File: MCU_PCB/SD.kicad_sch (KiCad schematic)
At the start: 2 parts

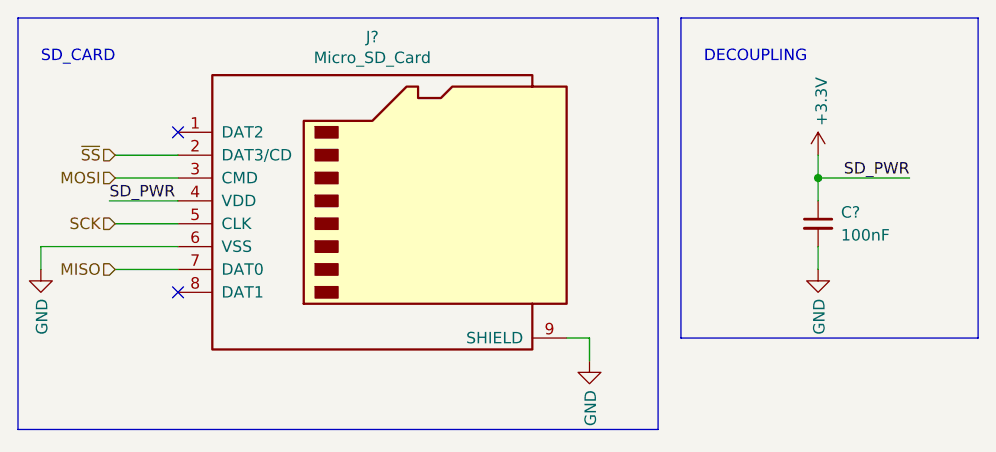
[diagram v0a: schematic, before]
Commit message: 0.1v MCU KiCad
Aesthetics needs to be improved.
Trace width needs to be changed.
More sufficient grounding.
Component placement could be changed.
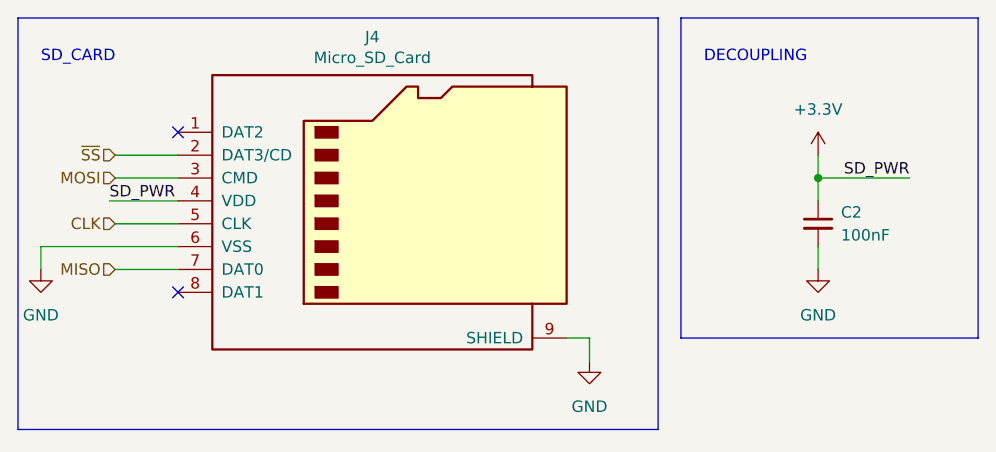
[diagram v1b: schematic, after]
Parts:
- C2: renamed from C?; footprint (none) -> Capacitor_SMD:C_0402_1005Metric
- J4: renamed from J?; footprint Borta_Dators:Micro_SD -> footprints:Micro_SD
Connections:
- net SCK renamed CLK
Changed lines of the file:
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@@
     (effects (font (size 1.27 1.27)) (justify right))
   )
-  (hierarchical_label "SCK" (shape input) (at 26.035 38.1 180)
+  (hierarchical_label "CLK" (shape input) (at 26.035 38.1 180)
     (effects (font (size 1.27 1.27)) (justify right))
   )
@@
   )
   (symbol (lib_id "power:+3.3V") (at 104.14 30.48 0) (unit 1)
-    (in_bom yes) (on_board yes)
-    (property "Reference" "#PWR?" (id 0) (at 104.14 34.29 0)
+    (in_bom yes) (on_board yes) (fields_autoplaced)
+    (property "Reference" "#PWR0113" (id 0) (at 104.14 34.29 0)
       (effects (font (size 1.27 1.27)) hide)
     )
-    (property "Value" "+3.3V" (id 1) (at 104.521 27.2288 90)
-      (effects (font (size 1.27 1.27)) (justify left))
-    )
+    (property "Value" "+3.3V" (id 1) (at 104.14 25.4 0))
     (property "Footprint" "" (id 2) (at 104.14 30.48 0)
       (effects (font (size 1.27 1.27)) hide)
@@
   )
   (symbol (lib_id "power:GND") (at 104.14 43.18 0) (unit 1)
-    (in_bom yes) (on_board yes)
-    (property "Reference" "#PWR?" (id 0) (at 104.14 49.53 0)
+    (in_bom yes) (on_board yes) (fields_autoplaced)
+    (property "Reference" "#PWR0110" (id 0) (at 104.14 49.53 0)
       (effects (font (size 1.27 1.27)) hide)
     )
-    (property "Value" "GND" (id 1) (at 104.267 46.4312 90)
-      (effects (font (size 1.27 1.27)) (justify right))
-    )
+    (property "Value" "GND" (id 1) (at 104.14 48.26 0))
     (property "Footprint" "" (id 2) (at 104.14 43.18 0)
       (effects (font (size 1.27 1.27)) hide)
@@
   (symbol (lib_id "Device:C_Small") (at 104.14 38.1 0) (unit 1)
     (in_bom yes) (on_board yes) (fields_autoplaced)
-    (property "Reference" "C?" (id 0) (at 106.68 36.8362 0)
+    (property "Reference" "C2" (id 0) (at 106.68 36.8362 0)
       (effects (font (size 1.27 1.27)) (justify left))
     )
@@
       (effects (font (size 1.27 1.27)) (justify left))
     )
-    (property "Footprint" "" (id 2) (at 104.14 38.1 0)
+    (property "Footprint" "Capacitor_SMD:C_0402_1005Metric" (id 2) (at 104.14 38.1 0)
       (effects (font (size 1.27 1.27)) hide)
     )
@@
   (symbol (lib_id "Connector:Micro_SD_Card") (at 55.88 35.56 0) (unit 1)
     (in_bom yes) (on_board yes)
-    (property "Reference" "J?" (id 0) (at 54.61 17.3482 0))
+    (property "Reference" "J4" (id 0) (at 54.61 17.3482 0))
     (property "Value" "Micro_SD_Card" (id 1) (at 54.61 19.6596 0))
-    (property "Footprint" "Borta_Dators:Micro_SD" (id 2) (at 85.09 27.94 0)
+    (property "Footprint" "footprints:Micro_SD" (id 2) (at 85.09 27.94 0)
       (effects (font (size 1.27 1.27)) hide)
     )
@@
   )
   (symbol (lib_id "power:GND") (at 17.78 43.18 0) (unit 1)
-    (in_bom yes) (on_board yes)
-    (property "Reference" "#PWR?" (id 0) (at 17.78 49.53 0)
+    (in_bom yes) (on_board yes) (fields_autoplaced)
+    (property "Reference" "#PWR0111" (id 0) (at 17.78 49.53 0)
       (effects (font (size 1.27 1.27)) hide)
     )
-    (property "Value" "GND" (id 1) (at 17.907 46.4312 90)
-      (effects (font (size 1.27 1.27)) (justify right))
-    )
+    (property "Value" "GND" (id 1) (at 17.78 48.26 0))
     (property "Footprint" "" (id 2) (at 17.78 43.18 0)
       (effects (font (size 1.27 1.27)) hide)
@@
   )
   (symbol (lib_id "power:GND") (at 78.74 53.34 0) (unit 1)
-    (in_bom yes) (on_board yes)
-    (property "Reference" "#PWR?" (id 0) (at 78.74 59.69 0)
+    (in_bom yes) (on_board yes) (fields_autoplaced)
+    (property "Reference" "#PWR0112" (id 0) (at 78.74 59.69 0)
       (effects (font (size 1.27 1.27)) hide)
     )
-    (property "Value" "GND" (id 1) (at 78.867 56.5912 90)
-      (effects (font (size 1.27 1.27)) (justify right))
-    )
+    (property "Value" "GND" (id 1) (at 78.74 58.42 0))
     (property "Footprint" "" (id 2) (at 78.74 53.34 0)
       (effects (font (size 1.27 1.27)) hide)
